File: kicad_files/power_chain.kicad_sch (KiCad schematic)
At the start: 14 parts, among them IC2 RT6150B-33GQW, J1 690-005-298-486

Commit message: header footprint generated
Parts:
- J1: footprint footprints:690-005-299-043 -> footprints:EDAC_690-005-298-486
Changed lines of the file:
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@@
       (effects (font (size 1.27 1.27)))
     )
-    (property "Footprint" "footprints:690-005-299-043" (at 61.595 91.44 0)
+    (property "Footprint" "footprints:EDAC_690-005-298-486" (at 61.595 91.44 0)
       (effects (font (size 1.27 1.27)) (justify left bottom) hide)
     )

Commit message: placement completed
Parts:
- C11: value C_Small -> 47uf; footprint (none) -> Capacitor_SMD:C_0805_2012Metric
- C12: footprint (none) -> Capacitor_SMD:C_0805_2012Metric
- D1: footprint SODFL3616X98N -> SamacSys_Parts:SODFL3616X98N
- IC2: footprint SON50P250X250X80-11N-D -> SamacSys_Parts:SON50P250X250X80-11N-D
- L1: footprint (none) -> SamacSys_Parts:DFE2016CKA1R0MP2
- R1, R2, R3, R4: footprint (none) -> Resistor_SMD:R_0201_0603Metric
- TP1, TP2, TP3, TP4: footprint (none) -> footprints:Custom_testpad
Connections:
- net GND: now also J1.SH1, J1.SH2, J1.SH3, J1.SH4, J1.SH5, J1.SH6; no longer J1.6 (S1), J1.7 (S2), J1.8 (S3), J1.9 (S4)
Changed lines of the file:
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@@
   (junction (at 200.66 83.82) (diameter 0) (color 0 0 0 0)
   )
+  (junction (at 80.645 114.935) (diameter 0) (color 0 0 0 0)
+  )
   (junction (at 100.33 83.82) (diameter 0) (color 0 0 0 0)
   )
@@
   )
   (junction (at 137.795 104.14) (diameter 0) (color 0 0 0 0)
+  )
+  (junction (at 80.645 111.76) (diameter 0) (color 0 0 0 0)
   )
   (no_connect (at 71.755 91.44))
@@
     (stroke (width 0) (type default))
   )
+  (wire (pts (xy 71.755 111.76) (xy 80.645 111.76))
+    (stroke (width 0) (type default))
+  )
   (wire (pts (xy 187.96 97.155) (xy 193.675 97.155))
     (stroke (width 0) (type default))
@@
     (stroke (width 0) (type default))
   )
+  (wire (pts (xy 80.645 111.76) (xy 80.645 114.935))
+    (stroke (width 0) (type default))
+  )
   (wire (pts (xy 143.51 95.25) (xy 137.795 95.25))
     (stroke (width 0) (type default))
@@
     (stroke (width 0) (type default))
   )
-  (wire (pts (xy 80.645 108.585) (xy 80.645 113.03))
+  (wire (pts (xy 80.645 108.585) (xy 80.645 111.76))
     (stroke (width 0) (type default))
   )
@@
     (stroke (width 0) (type default))
   )
+  (wire (pts (xy 80.645 114.935) (xy 80.645 117.475))
+    (stroke (width 0) (type default))
+  )
   (wire (pts (xy 200.66 95.25) (xy 200.66 103.505))
     (stroke (width 0) (type default))
@@
   )
   (wire (pts (xy 126.365 93.98) (xy 126.365 100.33))
+    (stroke (width 0) (type default))
+  )
+  (wire (pts (xy 71.755 114.935) (xy 80.645 114.935))
     (stroke (width 0) (type default))
   )
@@
   (symbol (lib_id "Device:C_Small") (at 200.66 92.71 0) (unit 1)
     (in_bom yes) (on_board yes) (dnp no) (fields_autoplaced)
-    (property "Reference" "C11" (at 203.2 92.0813 0)
-      (effects (font (size 1.27 1.27)) (justify left))
-    )
-    (property "Value" "C_Small" (at 203.2 94.6213 0)
-      (effects (font (size 1.27 1.27)) (justify left))
-    )
-    (property "Footprint" "" (at 200.66 92.71 0)
+    (property "Reference" "C11" (at 203.2 91.4463 0)
+      (effects (font (size 1.27 1.27)) (justify left))
+    )
+    (property "Value" "47uf" (at 203.2 93.9863 0)
+      (effects (font (size 1.27 1.27)) (justify left))
+    )
+    (property "Footprint" "Capacitor_SMD:C_0805_2012Metric" (at 200.66 92.71 0)
       (effects (font (size 1.27 1.27)) hide)
     )
@@
       (effects (font (size 1.27 1.27)))
     )
-    (property "Footprint" "SON50P250X250X80-11N-D" (at 200.025 66.04 0)
+    (property "Footprint" "SamacSys_Parts:SON50P250X250X80-11N-D" (at 200.025 66.04 0)
       (effects (font (size 1.27 1.27)) (justify left) hide)
     )
@@
       (effects (font (size 1.27 1.27)) (justify left))
     )
-    (property "Footprint" "" (at 84.455 93.98 0)
+    (property "Footprint" "footprints:Custom_testpad" (at 84.455 93.98 0)
       (effects (font (size 1.27 1.27)) hide)
     )
@@
     )
   )
-  (symbol (lib_id "power:GND") (at 80.645 113.03 0) (unit 1)
+  (symbol (lib_id "power:GND") (at 80.645 117.475 0) (unit 1)
     (in_bom yes) (on_board yes) (dnp no) (fields_autoplaced)
-    (property "Reference" "#PWR03" (at 80.645 119.38 0)
-      (effects (font (size 1.27 1.27)) hide)
-    )
-    (property "Value" "GND" (at 80.645 118.11 0)
-      (effects (font (size 1.27 1.27)))
-    )
-    (property "Footprint" "" (at 80.645 113.03 0)
-      (effects (font (size 1.27 1.27)) hide)
-    )
-    (property "Datasheet" "" (at 80.645 113.03 0)
+    (property "Reference" "#PWR03" (at 80.645 123.825 0)
+      (effects (font (size 1.27 1.27)) hide)
+    )
+    (property "Value" "GND" (at 80.645 122.555 0)
+      (effects (font (size 1.27 1.27)))
+    )
+    (property "Footprint" "" (at 80.645 117.475 0)
+      (effects (font (size 1.27 1.27)) hide)
+    )
+    (property "Datasheet" "" (at 80.645 117.475 0)
       (effects (font (size 1.27 1.27)) hide)
     )
@@
       (effects (font (size 1.27 1.27)) (justify left))
     )
-    (property "Footprint" "" (at 100.33 90.17 0)
+    (property "Footprint" "Resistor_SMD:R_0201_0603Metric" (at 100.33 90.17 0)
       (effects (font (size 1.27 1.27)) hide)
     )
@@
       (effects (font (size 1.27 1.27)))
     )
-    (property "Footprint" "" (at 165.1 71.755 0)
+    (property "Footprint" "SamacSys_Parts:DFE2016CKA1R0MP2" (at 165.1 71.755 0)
       (effects (font (size 1.27 1.27)) hide)
     )
@@
       (effects (font (size 1.27 1.27)) (justify left))
     )
-    (property "Footprint" "" (at 100.33 100.33 0)
+    (property "Footprint" "Resistor_SMD:R_0201_0603Metric" (at 100.33 100.33 0)
       (effects (font (size 1.27 1.27)) hide)
     )
@@
       (effects (font (size 1.27 1.27)) (justify left))
     )
-    (property "Footprint" "" (at 84.455 91.44 0)
+    (property "Footprint" "footprints:Custom_testpad" (at 84.455 91.44 0)
       (effects (font (size 1.27 1.27)) hide)
     )
@@
       (effects (font (size 1.27 1.27)) (justify left))
     )
-    (property "Footprint" "" (at 132.715 89.535 0)
+    (property "Footprint" "Capacitor_SMD:C_0805_2012Metric" (at 132.715 89.535 0)
       (effects (font (size 1.27 1.27)) hide)
     )
@@
     (pin "4")
     (pin "5")
-    (pin "6")
-    (pin "7")
-    (pin "8")
-    (pin "9")
+    (pin "SH1")
+    (pin "SH2")
+    (pin "SH3")
+    (pin "SH4")
+    (pin "SH5")
+    (pin "SH6")
     (instances
       (project "RP2040_Breakout"
@@
       (effects (font (size 1.27 1.27)) (justify right))
     )
-    (property "Footprint" "" (at 139.7 107.315 0)
+    (property "Footprint" "footprints:Custom_testpad" (at 139.7 107.315 0)
       (effects (font (size 1.27 1.27)) hide)
     )
@@
       (effects (font (size 1.27 1.27)) (justify left))
     )
-    (property "Footprint" "" (at 91.44 104.775 0)
+    (property "Footprint" "footprints:Custom_testpad" (at 91.44 104.775 0)
       (effects (font (size 1.27 1.27)) hide)
     )
@@
       (effects (font (size 1.27 1.27)) (justify left))
     )
-    (property "Footprint" "" (at 137.795 107.95 0)
+    (property "Footprint" "Resistor_SMD:R_0201_0603Metric" (at 137.795 107.95 0)
       (effects (font (size 1.27 1.27)) hide)
     )
@@
       (effects (font (size 1.27 1.27)))
     )
-    (property "Footprint" "SODFL3616X98N" (at 110.49 83.82 0)
+    (property "Footprint" "SamacSys_Parts:SODFL3616X98N" (at 110.49 83.82 0)
       (effects (font (size 1.27 1.27)) (justify left) hide)
     )
@@
       (effects (font (size 1.27 1.27)) (justify left))
     )
-    (property "Footprint" "" (at 126.365 91.44 0)
-      (effects (font (size 1.27 1.27)) hide)
-    )
+    (property "Footprint" "Resistor_SMD:R_0201_0603Metric" (at 126.365 91.44 0)
+      (effects (font (size 1.27 1.27)) hide)
+    )

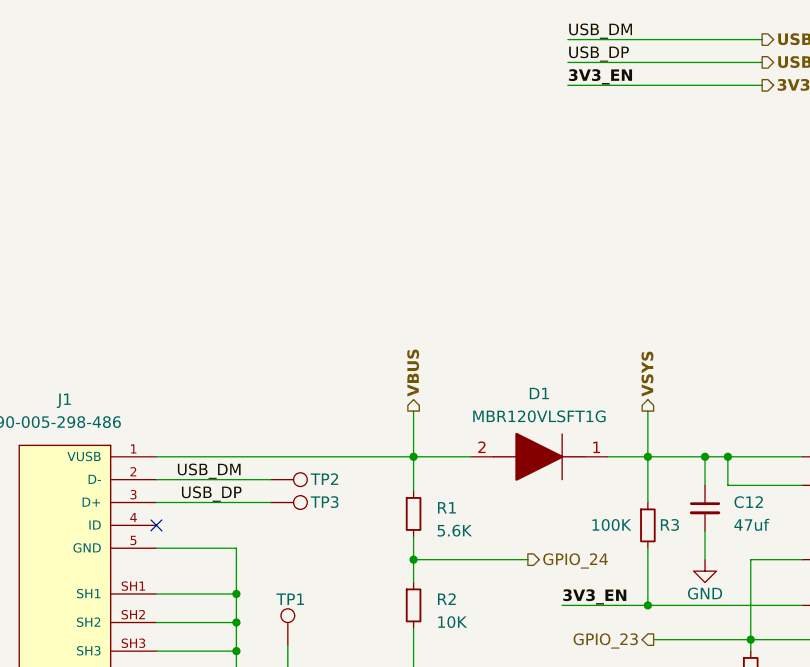
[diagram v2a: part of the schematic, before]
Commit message: initial routing started
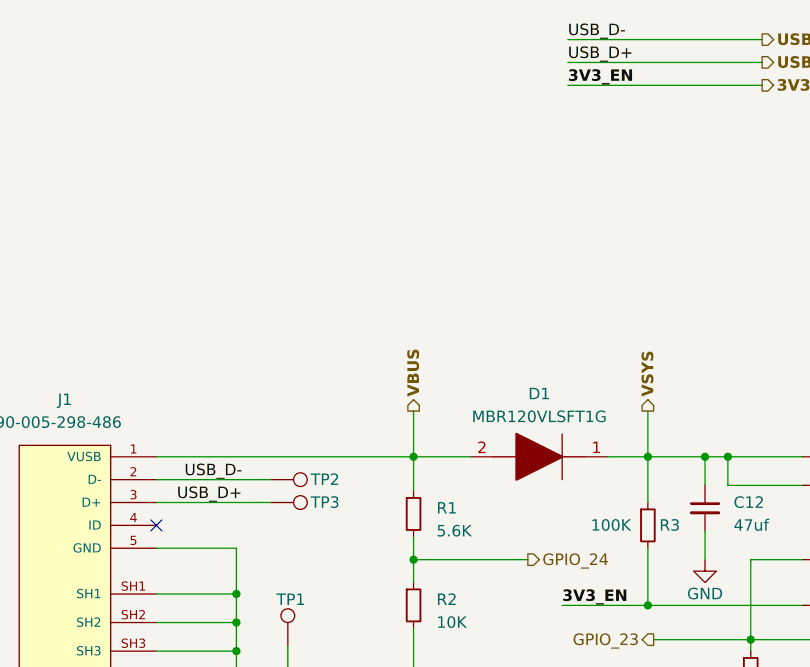
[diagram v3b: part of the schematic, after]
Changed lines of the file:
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@@
     (effects (font (size 1.27 1.27) bold) (justify left bottom))
   )
-  (label "USB_DM" (at 117.475 37.465 0) (fields_autoplaced)
+  (label "USB_D-" (at 117.475 37.465 0) (fields_autoplaced)
     (effects (font (size 1.27 1.27)) (justify left bottom))
   )
-  (label "USB_DM" (at 81.28 86.36 180) (fields_autoplaced)
+  (label "USB_D-" (at 81.28 86.36 180) (fields_autoplaced)
     (effects (font (size 1.27 1.27)) (justify right bottom))
   )
-  (label "USB_DP" (at 117.475 40.005 0) (fields_autoplaced)
+  (label "USB_D+" (at 117.475 40.005 0) (fields_autoplaced)
     (effects (font (size 1.27 1.27)) (justify left bottom))
   )
@@
     (effects (font (size 1.27 1.27) bold) (justify left bottom))
   )
-  (label "USB_DP" (at 81.28 88.9 180) (fields_autoplaced)
+  (label "USB_D+" (at 81.28 88.9 180) (fields_autoplaced)
     (effects (font (size 1.27 1.27)) (justify right bottom))
   )
